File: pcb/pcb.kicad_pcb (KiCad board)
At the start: 2 copper layers, 21.6 x 12.7 mm, 0 parts

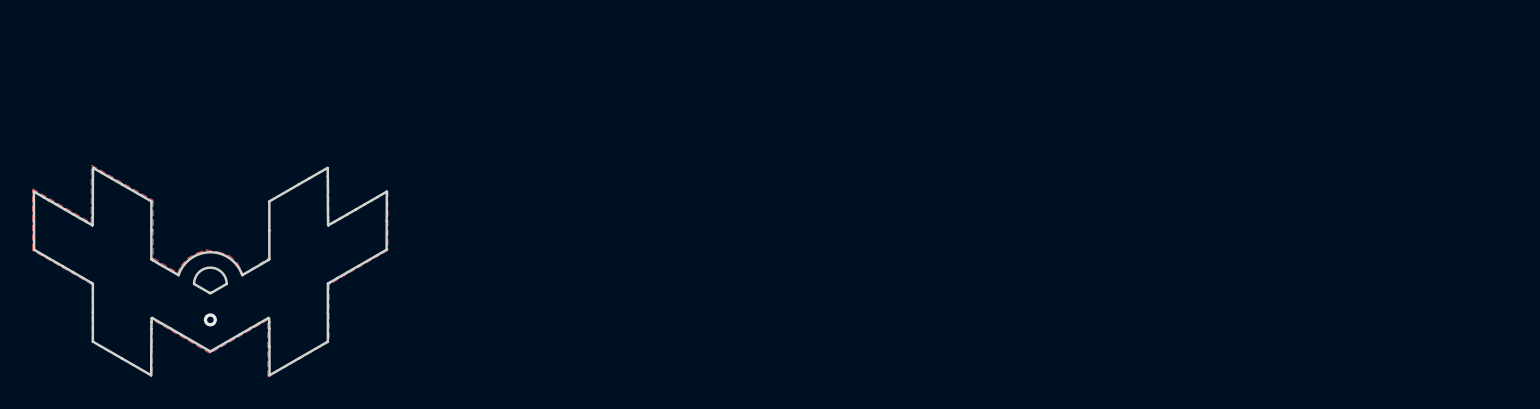
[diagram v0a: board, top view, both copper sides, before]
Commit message: Redraw edge.cuts and place footrpint for plated pattern
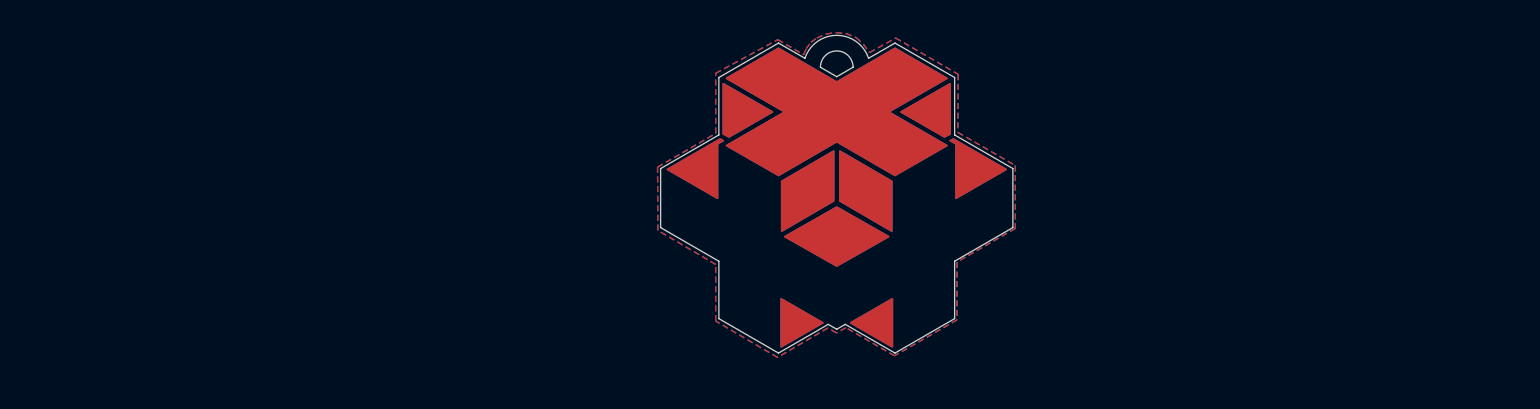
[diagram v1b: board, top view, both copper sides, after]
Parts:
- added REF**: Charm, Used_Footprints:Charm, B.Cu at (187.9, 100.5)
- added REF**: Charm, Used_Footprints:Charm, F.Cu at (187.9, 100.5)
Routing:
- net (no net): vias 1 -> 0
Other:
- board size 21.6 x 12.7 mm -> 21.6 x 19.5 mm

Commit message: Make a panel and remove old gerber files
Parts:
- added REF**: panelhole, keyboard_parts:panelhole, F.Cu at (207.2, 101.3)
- added REF**: panelhole, keyboard_parts:panelhole, F.Cu at (207.2, 99.0)
- added REF**: panelhole, keyboard_parts:panelhole, F.Cu at (207.2, 100.2)
- added REF**: panelhole, keyboard_parts:panelhole, F.Cu at (198.8, 101.3)
- added REF**: panelhole, keyboard_parts:panelhole, F.Cu at (198.8, 100.1)
- added REF**: panelhole, keyboard_parts:panelhole, F.Cu at (198.8, 98.9)
- added REF**: Charm, Used_Footprints:Charm, F.Cu at (218.1, 100.5)
- added REF**: Charm, Used_Footprints:Charm, B.Cu at (218.1, 100.5)
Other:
- board size 21.6 x 19.5 mm -> 51.7 x 19.5 mm
